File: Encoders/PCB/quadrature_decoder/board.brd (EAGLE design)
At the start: 84.8 x 55.9 mm, 14 parts, among them IC1 LFLS7366R, IC2 LFLS7366R, IC3 LFLS7366R, IC4 LFLS7366R, IC5 LFLS7366R, IC6 LFLS7366R

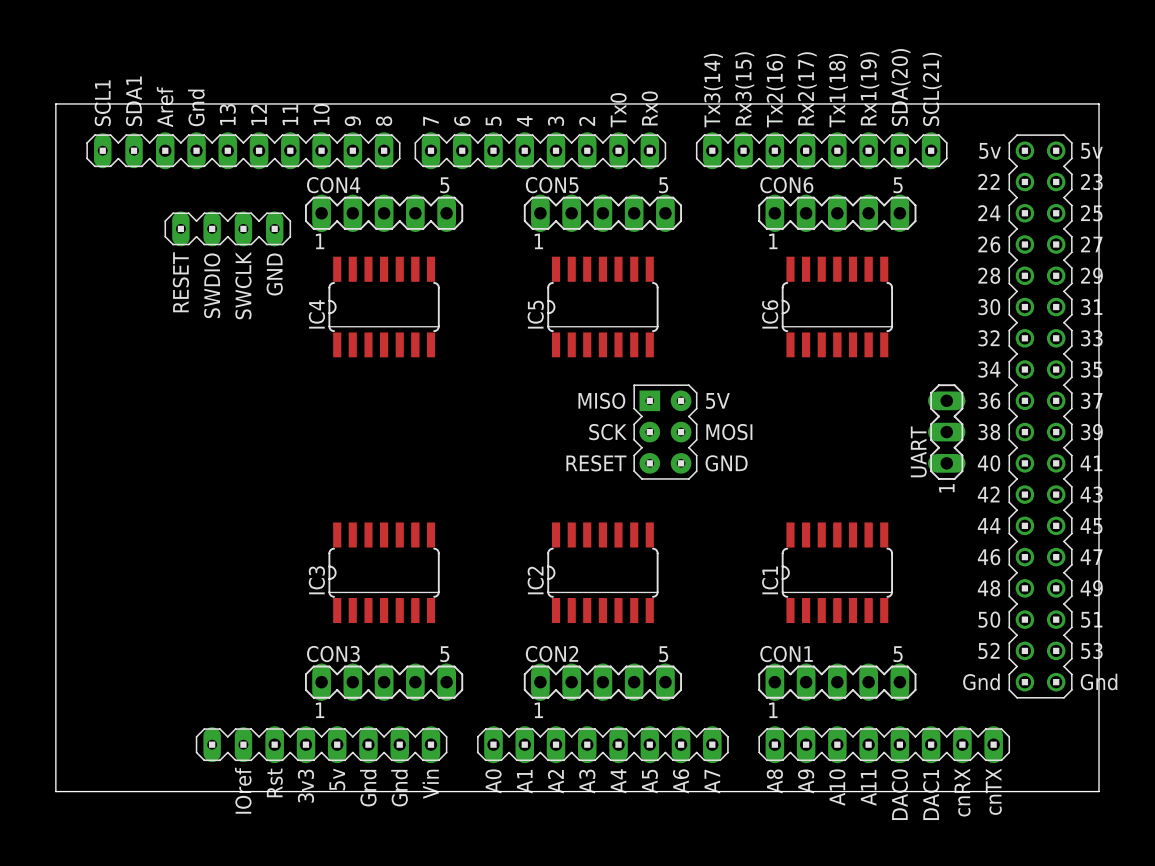
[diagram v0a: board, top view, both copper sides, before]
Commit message: changed pcb libs.
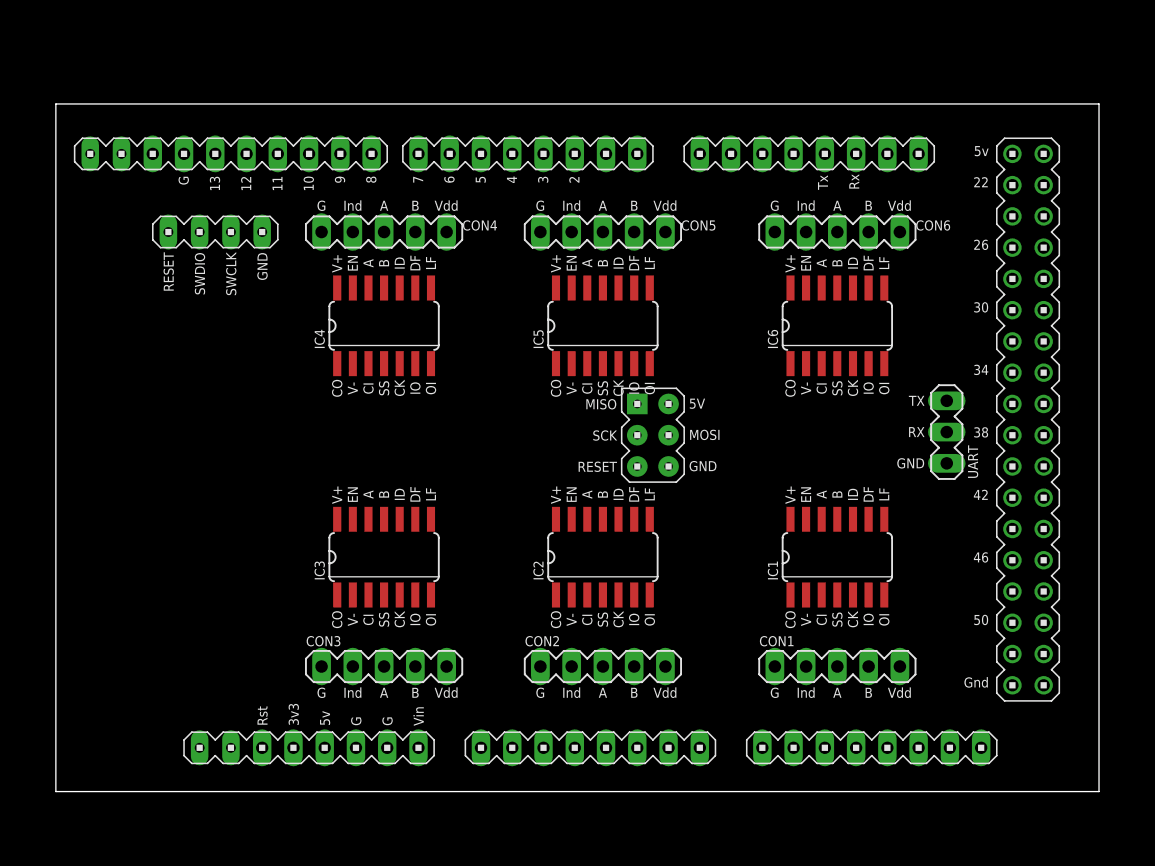
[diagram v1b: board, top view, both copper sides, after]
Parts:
- removed U$7: DUE(NORMAL), DUElib130425:DUE(NORMAL)
- added U$1: DUE(ENCODER), DUElib130425:DUE(ENCODER)
- CON1, CON2, CON3: device con-lstb:MA05-1 -> encoder_project:MA05-1
- CON4, CON5, CON6: device con-lstb:MA05-1 -> encoder_project:MA05-1(BOTTOM)
- UART: device con-lstb:MA03-1 -> encoder_project:MA03-1
- moved CON4 1.52 mm to (29.2, 46.7)
- moved CON5 1.52 mm to (47.0, 46.7)
- moved CON6 1.52 mm to (66.0, 46.7)
- moved IC4 1.52 mm to (29.2, 39.1)
- moved IC5 1.52 mm to (47.0, 39.1)
- moved IC6 1.52 mm to (66.0, 39.1)
- moved CON1 1.27 mm to (66.0, 11.4)
- moved CON2 1.27 mm to (47.0, 11.4)
- moved CON3 1.27 mm to (29.2, 11.4)
- moved IC1 1.27 mm to (66.0, 20.3)
- moved IC2 1.27 mm to (47.0, 20.3)
- moved IC3 1.27 mm to (29.2, 20.3)
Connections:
- net 3.3V: now also U$1.3V3; no longer U$7.3V3
- net 5V: now also U$1.5V; no longer U$7.5V
- net FCKI: now also U$1.DAC1; no longer U$7.DAC1
- net GND: now also U$1.5V_ICSP; no longer U$7.5V_ICSP
- net MISO: now also U$1.MISO_ICSP; no longer U$7.MISO_ICSP
- net MOSI: now also U$1.MOSI_ICSP; no longer U$7.MOSI_ICSP
- net N$3: now also U$1.TX1; no longer U$7.TX1
- net N$4: now also U$1.RX1; no longer U$7.RX1
- net SCK: now also U$1.SCK_ICSP; no longer U$7.SCK_ICSP
- net SS1: now also U$1.4; no longer U$7.4
- net SS2: now also U$1.5; no longer U$7.5
- net SS3: now also U$1.6; no longer U$7.6
- net SS4: now also U$1.7; no longer U$7.7
- net SS5: now also U$1.8; no longer U$7.8
- net SS6: now also U$1.9; no longer U$7.9

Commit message: new board
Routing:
- net GND: track 0.00 -> 196.1 mm, vias 0 -> 3
- net MOSI: track 0.00 -> 148.8 mm, vias 0 -> 3
- net FCKI: track 0.00 -> 138.1 mm, vias 0 -> 6
- net 5V: track 0.00 -> 137.7 mm
- net 3.3V: track 0.00 -> 134.3 mm, vias 0 -> 7
- net SCK: track 0.00 -> 103.2 mm, vias 0 -> 5
- net MISO: track 0.00 -> 97.9 mm, vias 0 -> 5
- net SS1: track 0.00 -> 80.9 mm, vias 0 -> 1
- net SS6: track 0.00 -> 53.3 mm
- net SS3: track 0.00 -> 47.4 mm, vias 0 -> 1
- net SS5: track 0.00 -> 47.0 mm
- net SS2: track 0.00 -> 44.1 mm, vias 0 -> 2
- net N$4: track 0.00 -> 25.8 mm
- net N$3: track 0.00 -> 24.2 mm
- net N$9: track 0.00 -> 23.6 mm
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
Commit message: rerouted
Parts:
- moved IC4 12.0 mm to (17.8, 35.6)
- moved IC5 12.0 mm to (35.6, 35.6)
- moved CON4 11.7 mm to (17.8, 44.5)
- moved CON5 11.7 mm to (35.6, 44.5)
- moved CON2 11.4 mm to (35.6, 11.4)
- moved CON3 11.4 mm to (17.8, 11.4)
- moved IC2 11.4 mm to (35.6, 20.3)
- moved IC3 11.4 mm to (17.8, 20.3)
- moved IC6 3.56 mm to (66.0, 35.6)
- moved CON6 2.29 mm to (66.0, 44.5)
- moved U$1 1.63 mm to (62.2, 21.3)
- moved UART 1.52 mm to (74.9, 29.0)
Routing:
- net MISO: track 97.9 -> 202.1 mm, vias 5 -> 6
- net SCK: track 103.2 -> 171.1 mm, vias 5 -> 3
- net SS1: track 80.9 -> 48.8 mm, vias 1 -> 2
- net SS2: track 44.1 -> 68.5 mm, vias 2 -> 0
- net SS5: track 47.0 -> 22.8 mm
- net SS3: track 47.4 -> 64.9 mm
- net N$2: track 15.1 -> 27.6 mm, vias 1 -> 0
- net 5V: track 137.7 -> 147.7 mm
- net SS4: track 22.2 -> 32.2 mm
- net GND: track 196.1 -> 205.7 mm
- net N$9: track 23.6 -> 19.3 mm
- net 3.3V: track 134.3 -> 137.9 mm, vias 7 -> 8
- net N$12: track 23.3 -> 26.8 mm
- net FCKI: track 138.1 -> 141.5 mm, vias 6 -> 9
- net SS6: track 53.3 -> 56.1 mm
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
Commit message: updated board
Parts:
- moved CON1 2.54 mm to (63.5, 11.4)
- moved CON6 2.54 mm to (63.5, 44.5)
- moved IC1 2.54 mm to (63.5, 20.3)
- moved IC6 2.54 mm to (63.5, 35.6)
- moved UART 2.54 mm to (72.4, 29.0)
- moved CON3 2.54 mm to (15.2, 11.4)
- moved CON4 2.54 mm to (15.2, 44.5)
- moved IC3 2.54 mm to (15.2, 20.3)
- moved IC4 2.54 mm to (15.2, 35.6)
- moved CON2 2.54 mm to (33.0, 11.4)
- moved CON5 2.54 mm to (33.0, 44.5)
- moved IC2 2.54 mm to (33.0, 20.3)
- moved IC5 2.54 mm to (33.0, 35.6)
- moved U$1 2.54 mm to (59.7, 21.3)
